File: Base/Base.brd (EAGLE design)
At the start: 83.8 x 61 mm, 29 parts, among them U1 VREG-MIC5205-3.3V

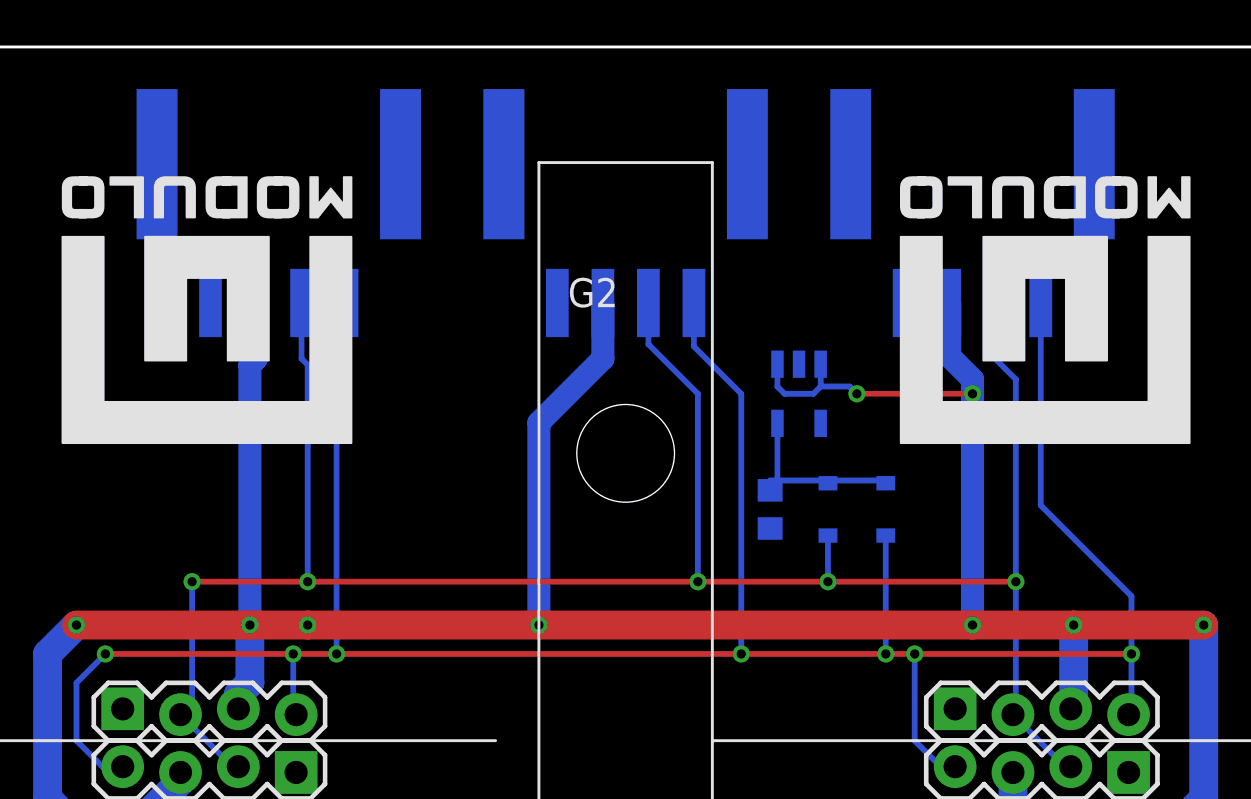
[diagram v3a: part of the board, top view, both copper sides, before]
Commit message: Various small tweaks based on testing and feedback from manufacturer.
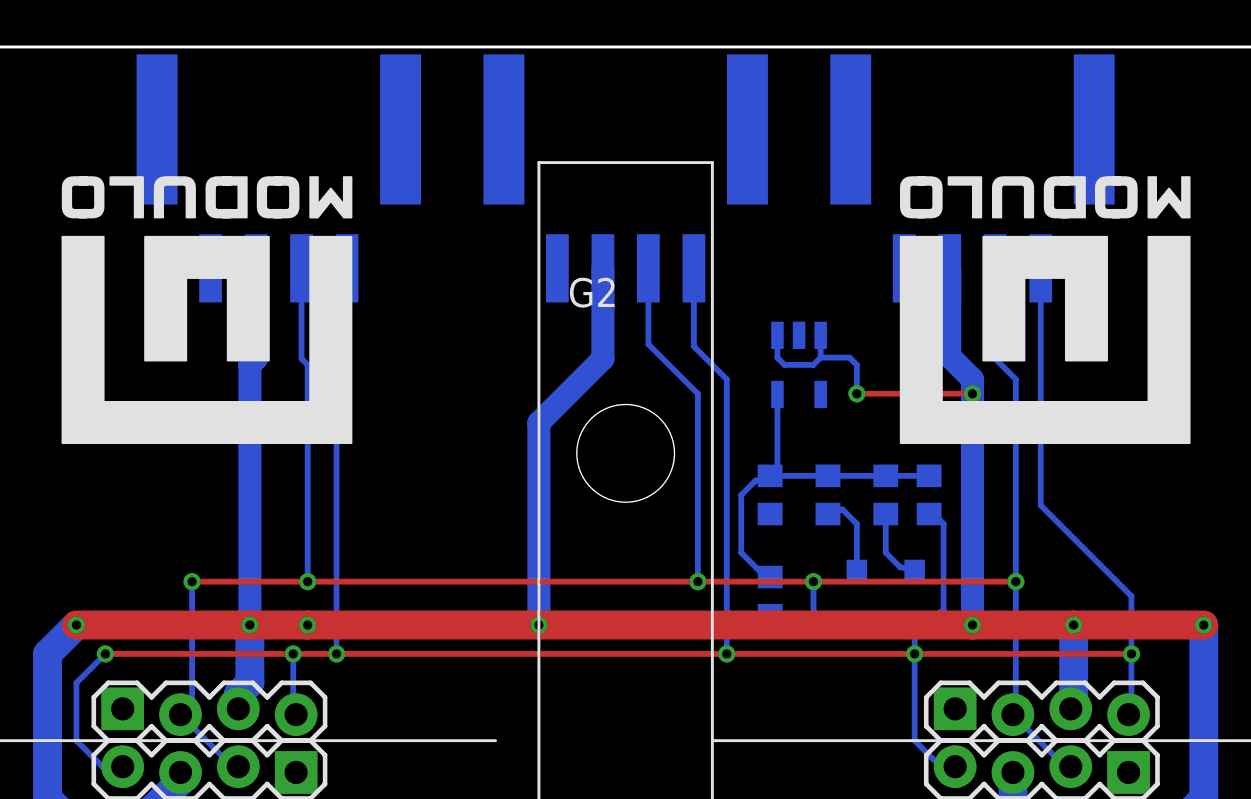
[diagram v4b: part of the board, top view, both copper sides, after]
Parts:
- added R1, R2: 12Ω, Modulo:0603
- added R3, R4: 5kΩ, Modulo:0603
- moved D1 4.02 mm to (52.1, 36.8)
- moved D2 4.02 mm to (54.6, 36.8)
- moved U1 1.27 mm to (49.5, 47.0)
- moved C1 0.63 mm to (48.3, 41.3)
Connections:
- new net N$1: D2.C, R2.1
- new net N$3: D1.C, R1.1
- net 3.3V: now also R1.2, R2.2, R3.2, R4.2; no longer D1.C, D2.C
- net SCL: now also R3.1
- net SDA: now also R4.1
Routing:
- net SDA: track 95.5 -> 104.4 mm
- net 3.3V: track 8.81 -> 16.6 mm
- net SCL: track 117.6 -> 124.3 mm, vias 7 -> 6
- net VCC: track 146.5 -> 152.3 mm
- net N$3: track 0.00 -> 3.59 mm
- net N$1: track 0.00 -> 3.25 mm

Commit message: Various minor tweaks based on testing and feedback from manufacturer
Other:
- board text added: "v1"
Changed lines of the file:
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@@
 <wire x1="83.82" y1="0" x2="83.82" y2="60.96" width="0.127" layer="20"/>
 <wire x1="83.82" y1="60.96" x2="0" y2="60.96" width="0.127" layer="20"/>
+<text x="82.55" y="6.35" size="1.524" layer="22" rot="MR0">v1</text>
 </plain>
 <attributes>

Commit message: Added unique board prefixes to part numbers due to CM requirements
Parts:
- added 2-FOOT1, 2-FOOT2, 2-FOOT3, 2-FOOT4: FOOT, Modulo:FOOT
- renumbered C1 to 2-C1, D1 to 2-D1, D2 to 2-D2, F1 to 2-F1, F2 to 2-F2, G1 to 2-G1, G2 to 2-G2, G3 to 2-G3, JP1 to 2-JP1, JP2 to 2-JP2, JP3 to 2-JP3, JP4 to 2-JP4, JP5 to 2-JP5, JP6 to 2-JP6, JP7 to 2-JP7, R1 to 2-R1, R2 to 2-R2, R3 to 2-R3, R4 to 2-R4, U1 to 2-U1
